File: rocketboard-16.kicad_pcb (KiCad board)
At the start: 2 copper layers, 86.2 x 105.8 mm, 110 parts, among them J1 SWD, K1 MX_RGB, K10 MX_RGB, K11 MX_RGB, K12 MX_RGB, K13 MX_RGB, K14 MX_RGB, K15 MX_RGB, K16 MX_RGB, K2 MX_RGB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

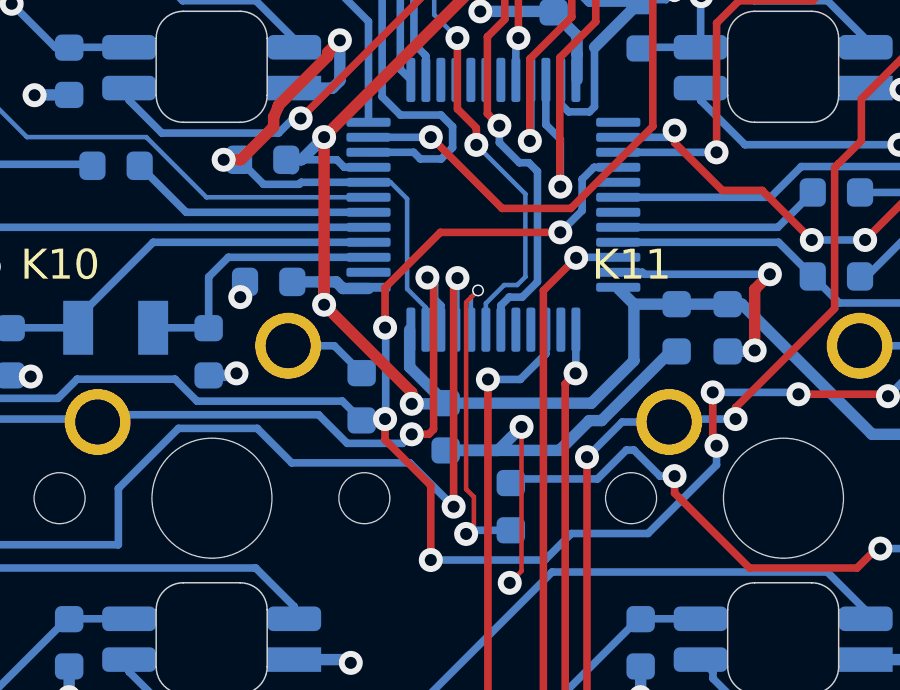
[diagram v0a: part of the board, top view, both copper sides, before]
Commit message: Updated symbols and footprints to use project specific files (portability). Changed one via, was only one smaller than rest.
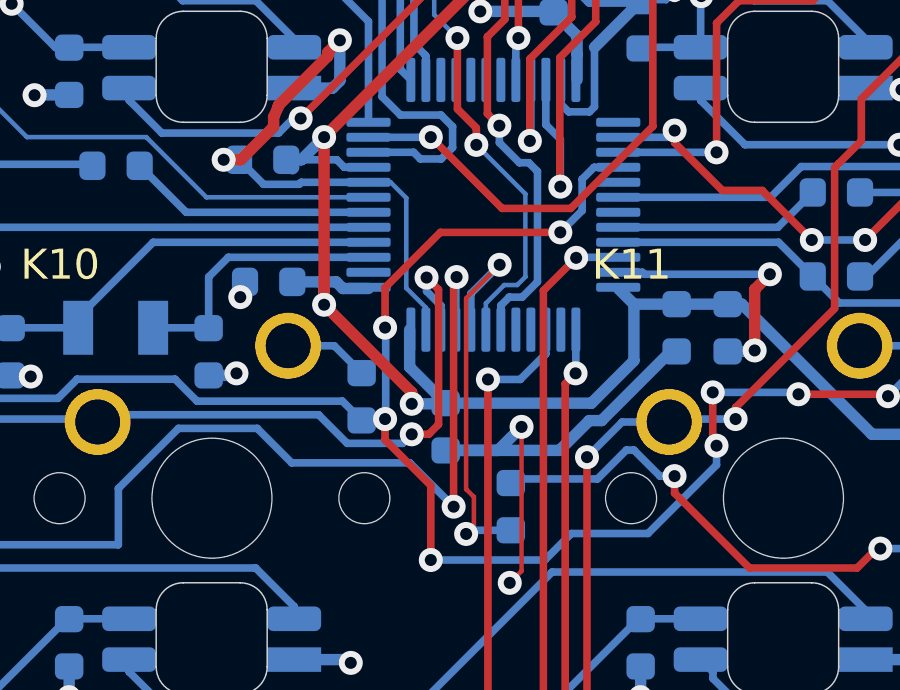
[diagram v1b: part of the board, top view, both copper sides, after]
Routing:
- net Net-(R8-Pad1): track 11.4 -> 13.8 mm

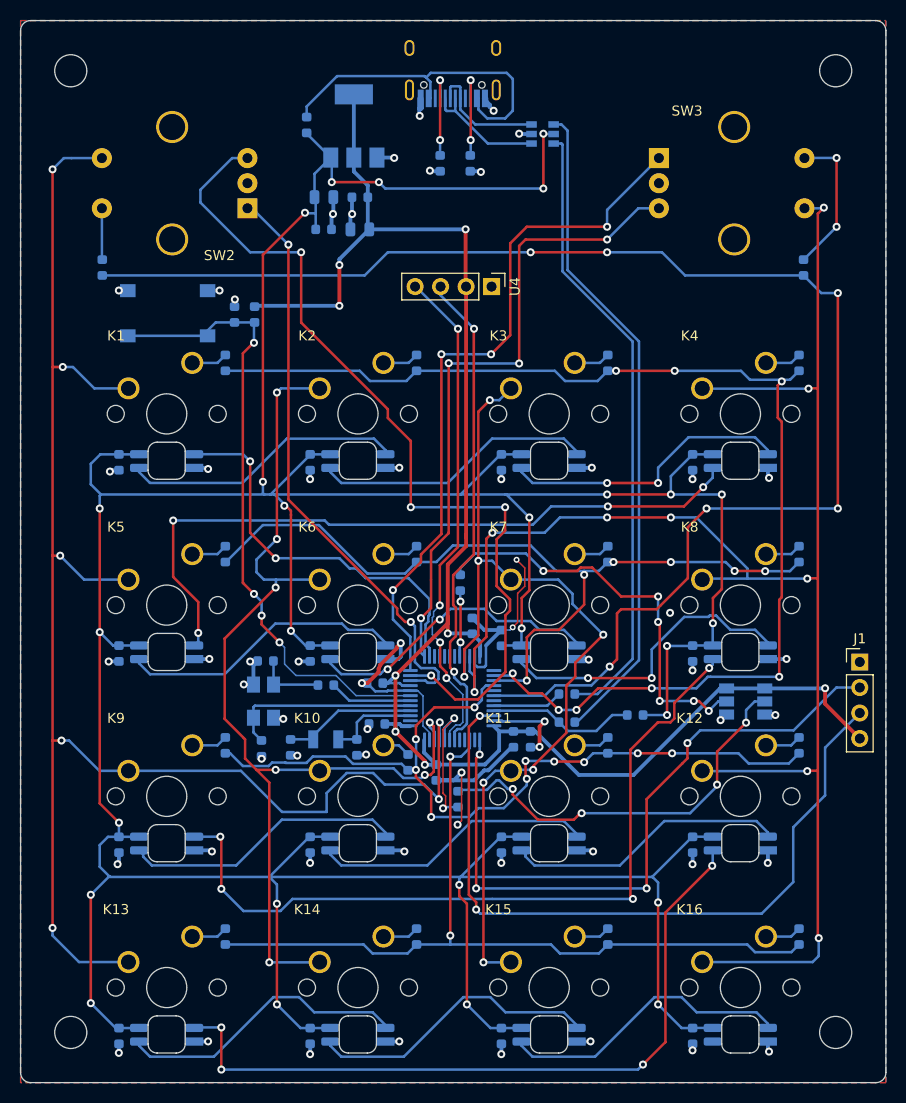
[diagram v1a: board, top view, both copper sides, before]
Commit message: Updated schematic and pcb as I found specific parts for BOM, now board needs routing for the diodes on the switches. Created a BOM spreadsheet for manual entry of part numbers, venders, prices, etc.
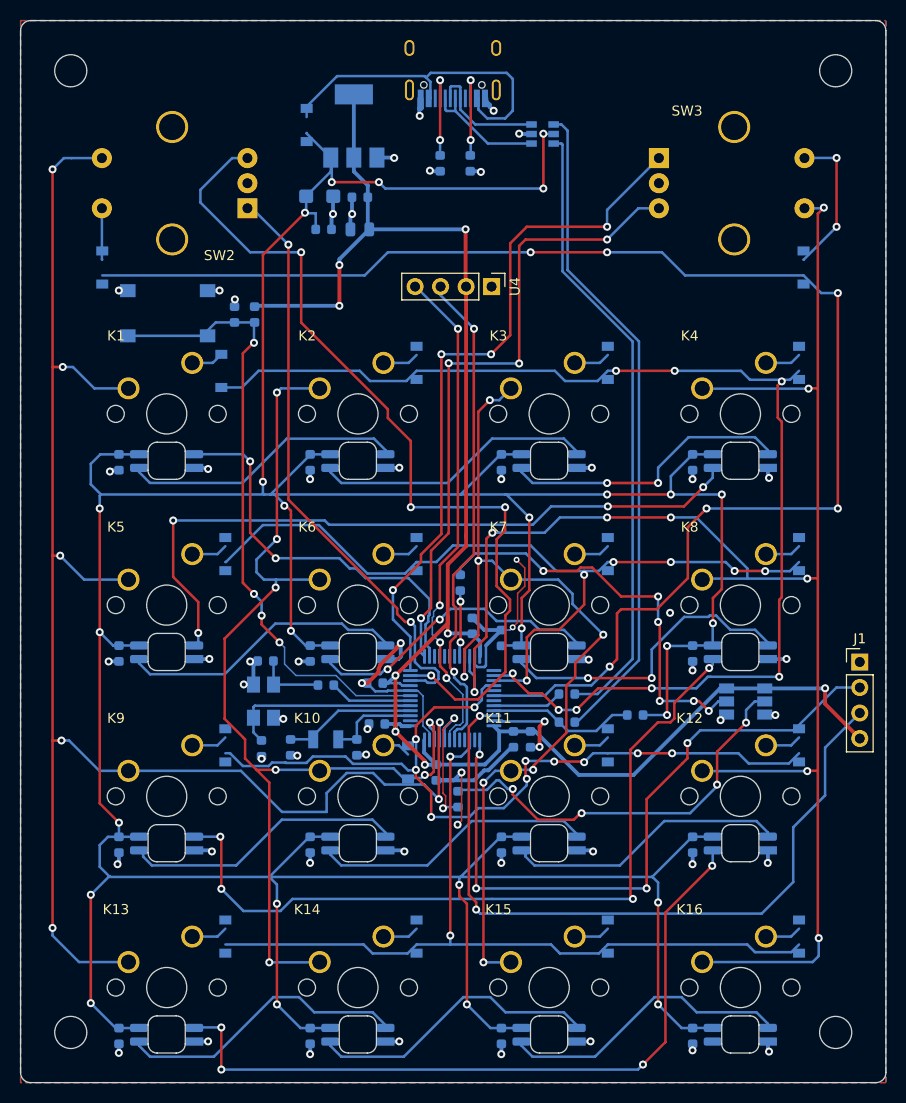
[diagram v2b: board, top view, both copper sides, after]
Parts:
- C1, C2: value 27p -> 20p
- C10: footprint Capacitor_SMD:C_0805_2012Metric -> Capacitor_Tantalum_SMD:CP_EIA-3216-10_Kemet-I
- C12, C3: value 12.5p -> 10p
- D1, D10, D11, D12, D13, D14, D15, D16, D17, D18, D19, D2, D3, D4, D5, D6, D7, D8, D9: footprint Diode_SMD:D_0603_1608Metric -> Diode_SMD:D_SOD-123
- D20, D21, D22, D23, D24, D25, D26, D27, D28, D29, D30, D31, D32, D33, D34, D35: footprint josh-keyboard:DUMMY_SK6812MINI-E -> seth-keyboard:DUMMY_SK6812MINI-E
- K1, K10, K11, K12, K13, K14, K15, K16, K2, K3, K4, K5, K6, K7, K8, K9: footprint josh-keyboard:MX_KEYSWITCH_RGB_2D -> seth-keyboard:MX_KEYSWITCH_RGB_2D
- P1: footprint josh-connectors:USB_C_U262-161N-4BVC11 -> seth-connectors:USB_C_U262-161N-4BVC11
- R7: value 390 -> 1k
- SW2, SW3: footprint josh-buttons-switches:RotaryEncoder_Alps_EC11E-Switch_Vertical_H20mm_CircularMountingHoles -> seth-buttons:RotaryEncoder_Alps_EC11E-Switch_Vertical_H20mm_CircularMountingHoles
- moved D1 0.89 mm to (100.0, 80.4)
- moved C10 0.43 mm to (109.8, 63.0)
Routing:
- net ROW1: track 121.2 -> 122.3 mm

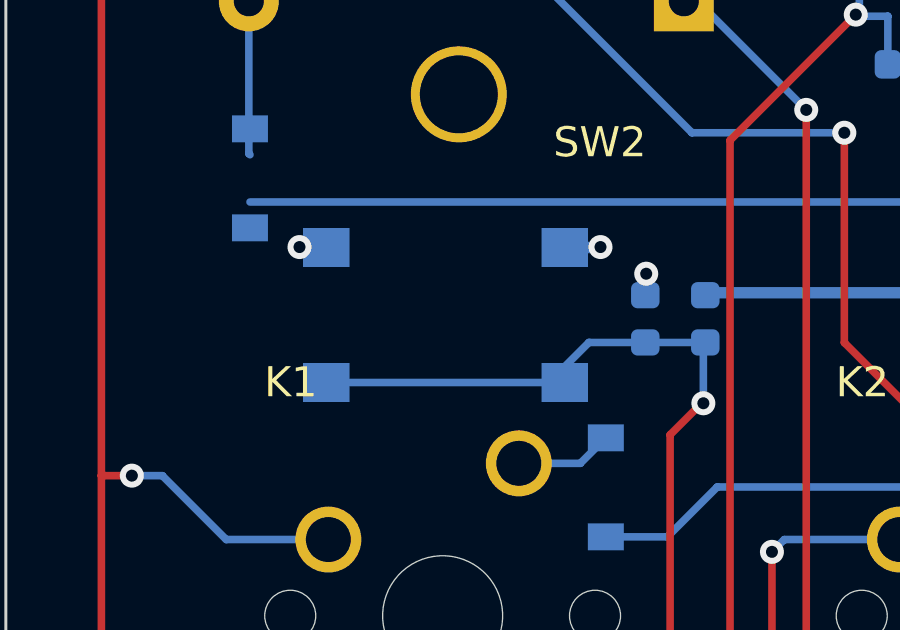
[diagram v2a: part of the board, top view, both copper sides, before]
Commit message: Finished adding items to the BOM, added a tactile switch from JLCPCB footprint instead of the one I had
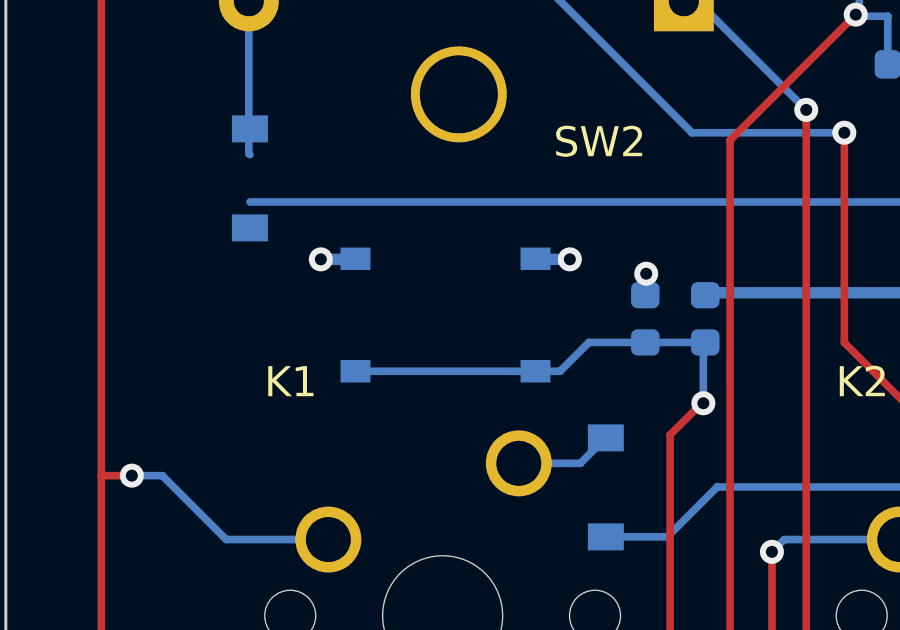
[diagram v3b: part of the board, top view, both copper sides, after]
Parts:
- SW1: footprint Button_Switch_SMD:SW_Push_1P1T_NO_6x6mm_H9.5mm -> seth-tactile-switch:SW_TS-1187A-B-A-B
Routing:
- net Net-(C31-Pad2): track 63.6 -> 62.2 mm
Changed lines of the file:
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@@
     (add_net VCC)
   )
+  (module seth-tactile-switch:SW_TS-1187A-B-A-B (layer B.Cu)
+    (at 94.656 74.655 180)
+    (fp_text reference SW1 (at -0.825 3.635) (layer B.SilkS)
+      (effects (font (size 1 1) (thickness 0.015)) (justify mirror))
+    )
+    (fp_text value SW_Push (at 6.795 -3.565) (layer B.Fab)
+      (effects (font (size 1 1) (thickness 0.015)) (justify mirror))
+    )
+    (fp_line (start 2.55 -2.55) (end 2.55 2.55) (layer B.Fab) (width 0.127))
+    (fp_line (start 2.55 2.55) (end -2.55 2.55) (layer B.Fab) (width 0.127))
+    (fp_line (start -2.55 2.55) (end -2.55 -2.55) (layer B.Fab) (width 0.127))
+    (fp_line (start -2.55 -2.55) (end 2.55 -2.55) (layer B.Fab) (width 0.127))
+    (fp_line (start 2.25 -2.55) (end -2.25 -2.55) (layer B.SilkS) (width 0.127))
+    (fp_line (start 2.25 2.55) (end -2.25 2.55) (layer B.SilkS) (width 0.127))
+    (fp_line (start -3.75 2.5) (end -3.75 1.25) (layer B.CrtYd) (width 0.05))
+    (fp_circle (center -4.25 1.875) (end -4.15 1.875) (layer B.SilkS) (width 0.2))
+    (fp_circle (center -4.25 1.875) (end -4.15 1.875) (layer B.Fab) (width 0.2))
+    (fp_line (start -2.55 1.18) (end -2.55 -1.18) (layer B.SilkS) (width 0.127))
+    (fp_line (start 2.55 -1.18) (end 2.55 1.18) (layer B.SilkS) (width 0.127))
+    (fp_line (start -2.8 1.25) (end -2.8 -1.25) (layer B.CrtYd) (width 0.05))
+    (fp_line (start -3.75 1.25) (end -2.8 1.25) (layer B.CrtYd) (width 0.05))
+    (fp_line (start -3.75 -1.25) (end -2.8 -1.25) (layer B.CrtYd) (width 0.05))
+    (fp_line (start -2.8 2.8) (end -2.8 2.5) (layer B.CrtYd) (width 0.05))
+    (fp_line (start -3.75 2.5) (end -2.8 2.5) (layer B.CrtYd) (width 0.05))
+    (fp_line (start 2.8 2.8) (end -2.8 2.8) (layer B.CrtYd) (width 0.05))
+    (fp_line (start 3.75 -2.5) (end 3.75 -1.25) (layer B.CrtYd) (width 0.05))
+    (fp_line (start 2.8 -2.8) (end 2.8 -2.5) (layer B.CrtYd) (width 0.05))
+    (fp_line (start 3.75 -2.5) (end 2.8 -2.5) (layer B.CrtYd) (width 0.05))
+    (fp_line (start -2.8 -2.8) (end 2.8 -2.8) (layer B.CrtYd) (width 0.05))
+    (fp_line (start 3.75 2.5) (end 3.75 1.25) (layer B.CrtYd) (width 0.05))
+    (fp_line (start 2.8 1.25) (end 2.8 -1.25) (layer B.CrtYd) (width 0.05))
+    (fp_line (start 3.75 1.25) (end 2.8 1.25) (layer B.CrtYd) (width 0.05))
+    (fp_line (start 3.75 -1.25) (end 2.8 -1.25) (layer B.CrtYd) (width 0.05))
+    (fp_line (start 2.8 2.8) (end 2.8 2.5) (layer B.CrtYd) (width 0.05))
+    (fp_line (start 3.75 2.5) (end 2.8 2.5) (layer B.CrtYd) (width 0.05))
+    (fp_line (start -3.75 -2.5) (end -3.75 -1.25) (layer B.CrtYd) (width 0.05))
+    (fp_line (start -2.8 -2.8) (end -2.8 -2.5) (layer B.CrtYd) (width 0.05))
+    (fp_line (start -3.75 -2.5) (end -2.8 -2.5) (layer B.CrtYd) (width 0.05))
+    (pad 1 smd rect (at -3 1.875 180) (size 1 0.75) (layers B.Cu B.Paste B.Mask)
+      (net 24 GND))
+    (pad 1 smd rect (at 3 1.875 180) (size 1 0.75) (layers B.Cu B.Paste B.Mask)
+      (net 24 GND))
+    (pad 2 smd rect (at -3 -1.875 180) (size 1 0.75) (layers B.Cu B.Paste B.Mask)
+      (net 85 "Net-(C31-Pad2)"))
+    (pad 2 smd rect (at 3 -1.875 180) (size 1 0.75) (layers B.Cu B.Paste B.Mask)
+      (net 85 "Net-(C31-Pad2)"))
+  )
   (module seth-buttons:RotaryEncoder_Alps_EC11E-Switch_Vertical_H20mm_CircularMountingHoles locked (layer F.Cu)
     (at 143.59 59.2)
@@
     )
   )
-  (module Button_Switch_SMD:SW_Push_1P1T_NO_6x6mm_H9.5mm (layer B.Cu)
-    (at 94.656 74.655 180)
-    (descr "tactile push button, 6x6mm e.g. PTS645xx series, height=9.5mm")
-    (tags "tact sw push 6mm smd")
-    (attr smd)
-    (fp_text reference SW1 (at 0 -4) (layer B.SilkS)
-      (effects (font (size 1 1) (thickness 0.15)) (justify mirror))
-    )
-    (fp_text value SW_Push (at 0 -4.15) (layer B.Fab)
-      (effects (font (size 1 1) (thickness 0.15)) (justify mirror))
-    )
-    (fp_line (start -3 3) (end -3 -3) (layer B.Fab) (width 0.1))
-    (fp_line (start -3 -3) (end 3 -3) (layer B.Fab) (width 0.1))
-    (fp_line (start 3 -3) (end 3 3) (layer B.Fab) (width 0.1))
-    (fp_line (start 3 3) (end -3 3) (layer B.Fab) (width 0.1))
-    (fp_line (start 5 -3.25) (end 5 3.25) (layer B.CrtYd) (width 0.05))
-    (fp_line (start -5 3.25) (end -5 -3.25) (layer B.CrtYd) (width 0.05))
-    (fp_line (start -5 -3.25) (end 5 -3.25) (layer B.CrtYd) (width 0.05))
-    (fp_line (start -5 3.25) (end 5 3.25) (layer B.CrtYd) (width 0.05))
-    (fp_line (start 3.23 3.23) (end 3.23 3.2) (layer B.SilkS) (width 0.12))
-    (fp_line (start 3.23 -3.23) (end 3.23 -3.2) (layer B.SilkS) (width 0.12))
-    (fp_line (start -3.23 -3.23) (end -3.23 -3.2) (layer B.SilkS) (width 0.12))
-    (fp_line (start -3.23 3.2) (end -3.23 3.23) (layer B.SilkS) (width 0.12))
-    (fp_line (start 3.23 1.3) (end 3.23 -1.3) (layer B.SilkS) (width 0.12))
-    (fp_line (start -3.23 3.23) (end 3.23 3.23) (layer B.SilkS) (width 0.12))
-    (fp_line (start -3.23 1.3) (end -3.23 -1.3) (layer B.SilkS) (width 0.12))
-    (fp_line (start -3.23 -3.23) (end 3.23 -3.23) (layer B.SilkS) (width 0.12))
-    (fp_circle (center 0 0) (end 1.75 0.05) (layer B.Fab) (width 0.1))
-    (fp_text user %R (at 0 4.05) (layer B.Fab)
-      (effects (font (size 1 1) (thickness 0.15)) (justify mirror))
-    )
-    (pad 2 smd rect (at 3.975 -2.25 180) (size 1.55 1.3) (layers B.Cu B.Paste B.Mask)
-      (net 85 "Net-(C31-Pad2)"))
-    (pad 1 smd rect (at 3.975 2.25 180) (size 1.55 1.3) (layers B.Cu B.Paste B.Mask)
-      (net 24 GND))
-    (pad 1 smd rect (at -3.975 2.25 180) (size 1.55 1.3) (layers B.Cu B.Paste B.Mask)
-      (net 24 GND))
-    (pad 2 smd rect (at -3.975 -2.25 180) (size 1.55 1.3) (layers B.Cu B.Paste B.Mask)
-      (net 85 "Net-(C31-Pad2)"))
-    (model ${KISYS3DMOD}/Button_Switch_SMD.3dshapes/SW_PUSH_6mm_H9.5mm.wrl
-      (at (xyz 0 0 0))
-      (scale (xyz 1 1 1))
-      (rotate (xyz 0 0 0))
-    )
-  )
   (module Resistor_SMD:R_0603_1608Metric (layer B.Cu)
     (at 124.8 59.721 270)
@@
   (segment (start 112.8625 64.9375) (end 113.03 64.77) (width 0.381) (layer B.Cu) (net 24))
   (segment (start 112.8625 66.3) (end 112.8625 64.9375) (width 0.381) (layer B.Cu) (net 24))
-  (via (at 99.822 72.39) (size 0.8) (drill 0.4) (layers F.Cu B.Cu) (net 24))
-  (segment (start 98.631 72.405) (end 99.807 72.405) (width 0.381) (layer B.Cu) (net 24))
-  (segment (start 99.807 72.405) (end 99.822 72.39) (width 0.381) (layer B.Cu) (net 24))
-  (via (at 89.789 72.39) (size 0.8) (drill 0.4) (layers F.Cu B.Cu) (net 24))
-  (segment (start 90.681 72.405) (end 89.804 72.405) (width 0.381) (layer B.Cu) (net 24))
-  (segment (start 89.804 72.405) (end 89.789 72.39) (width 0.381) (layer B.Cu) (net 24))
+  (via (at 98.8 72.8) (size 0.8) (drill 0.4) (layers F.Cu B.Cu) (net 24))
+  (via (at 90.5 72.8) (size 0.8) (drill 0.4) (layers F.Cu B.Cu) (net 24))
   (via (at 101.346 73.279) (size 0.8) (drill 0.4) (layers F.Cu B.Cu) (net 24))
   (segment (start 101.315 73.9945) (end 101.315 73.31) (width 0.381) (layer B.Cu) (net 24))
@@
   (segment (start 110.975 64.92) (end 111.125 64.77) (width 0.381) (layer B.Cu) (net 24))
   (segment (start 110.975 66.3) (end 110.975 64.92) (width 0.381) (layer B.Cu) (net 24))
+  (segment (start 91.636 72.8) (end 91.656 72.78) (width 0.381) (layer B.Cu) (net 24))
+  (segment (start 90.5 72.8) (end 91.636 72.8) (width 0.381) (layer B.Cu) (net 24))
+  (segment (start 97.676 72.8) (end 97.656 72.78) (width 0.381) (layer B.Cu) (net 24))
+  (segment (start 98.8 72.8) (end 97.676 72.8) (width 0.381) (layer B.Cu) (net 24))
   (segment (start 103.2 116.4125) (end 104 117.2125) (width 0.254) (layer B.Cu) (net 25))
   (segment (start 103.2 114.95) (end 103.2 116.4125) (width 0.254) (layer B.Cu) (net 25))
@@
   (segment (start 153.30137 144.29137) (end 154.45 145.44) (width 0.254) (layer B.Cu) (net 83))
   (segment (start 130.997 148.717) (end 137.227038 148.717) (width 0.254) (layer B.Cu) (net 83))
-  (segment (start 90.681 76.905) (end 98.631 76.905) (width 0.254) (layer B.Cu) (net 85))
-  (segment (start 98.631 76.905) (end 98.631 76.375) (width 0.254) (layer B.Cu) (net 85))
   (segment (start 99.4365 75.5695) (end 101.315 75.5695) (width 0.254) (layer B.Cu) (net 85))
-  (segment (start 98.631 76.375) (end 99.4365 75.5695) (width 0.254) (layer B.Cu) (net 85))
   (segment (start 101.315 75.5695) (end 103.315 75.5695) (width 0.254) (layer B.Cu) (net 85))
   (segment (start 113.424982 112.75) (end 111.418982 110.744) (width 0.1524) (layer B.Cu) (net 85))
@@
   (segment (start 103.251 75.6335) (end 103.315 75.5695) (width 0.254) (layer B.Cu) (net 85))
   (segment (start 103.251 77.597) (end 103.251 75.6335) (width 0.254) (layer B.Cu) (net 85))
+  (segment (start 91.656 76.53) (end 97.656 76.53) (width 0.254) (layer B.Cu) (net 85))
+  (segment (start 98.476 76.53) (end 99.4365 75.5695) (width 0.254) (layer B.Cu) (net 85))
+  (segment (start 97.656 76.53) (end 98.476 76.53) (width 0.254) (layer B.Cu) (net 85))
   (zone (net 24) (net_name GND) (layer F.Cu) (hatch edge 0.508)
     (connect_pads (clearance 0.508))
